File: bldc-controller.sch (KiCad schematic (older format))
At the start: 13 parts

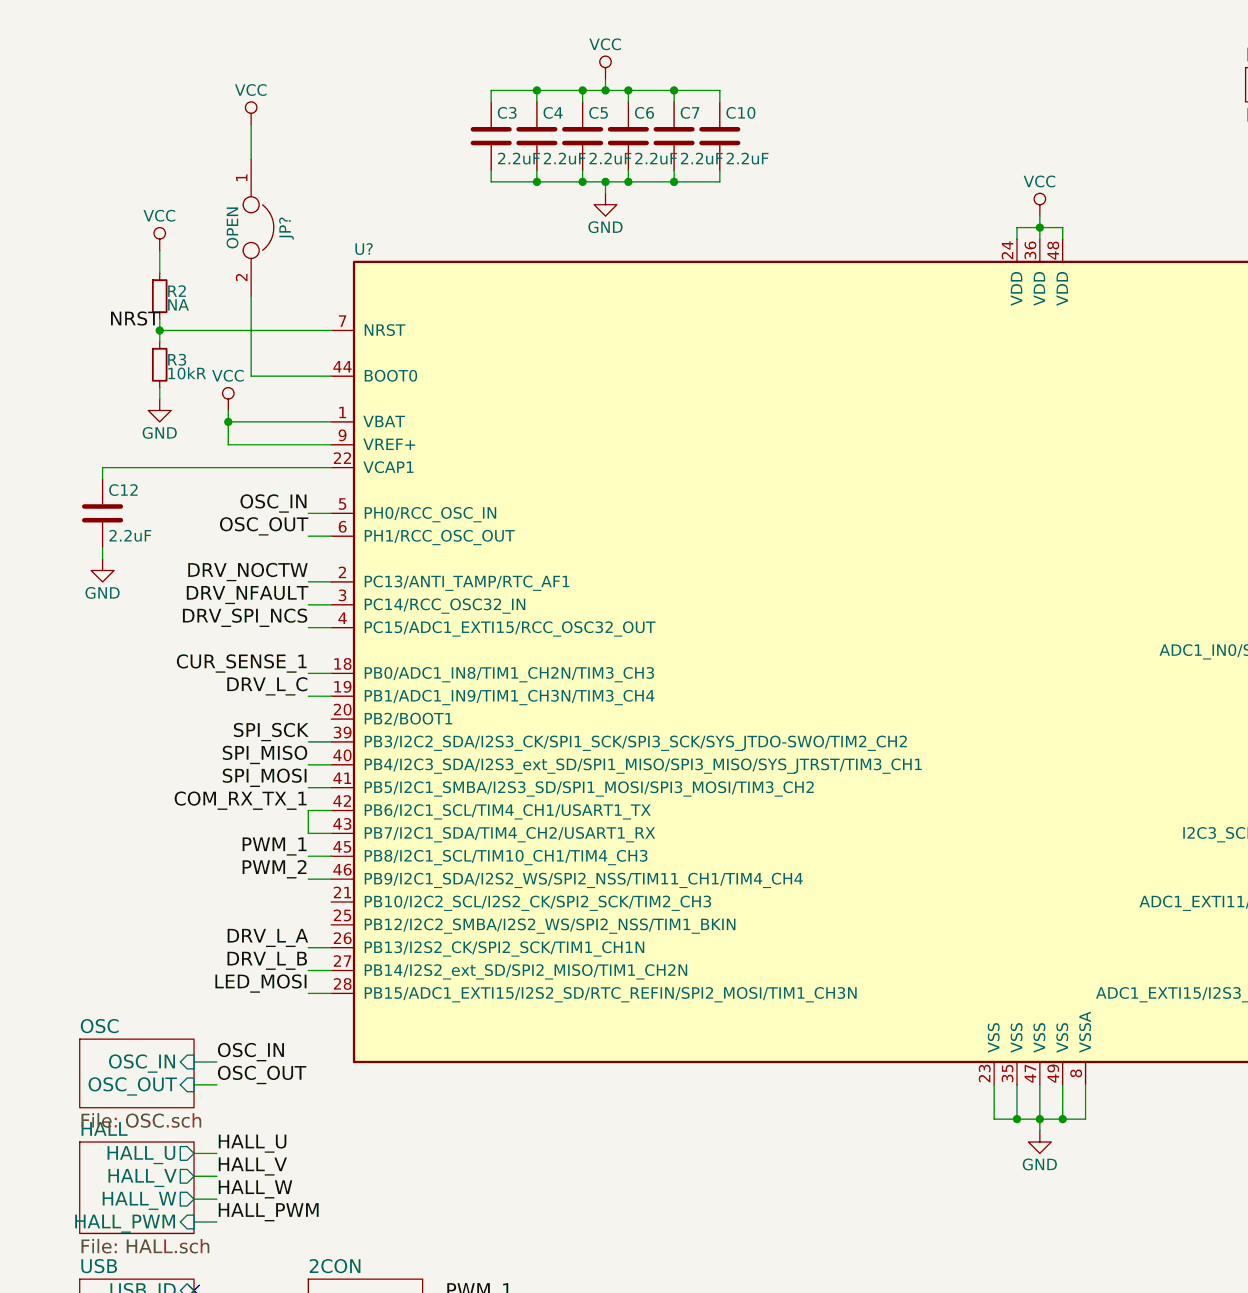
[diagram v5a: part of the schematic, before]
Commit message: changed the maximum outpul voltage of the RC-Filter to VPP
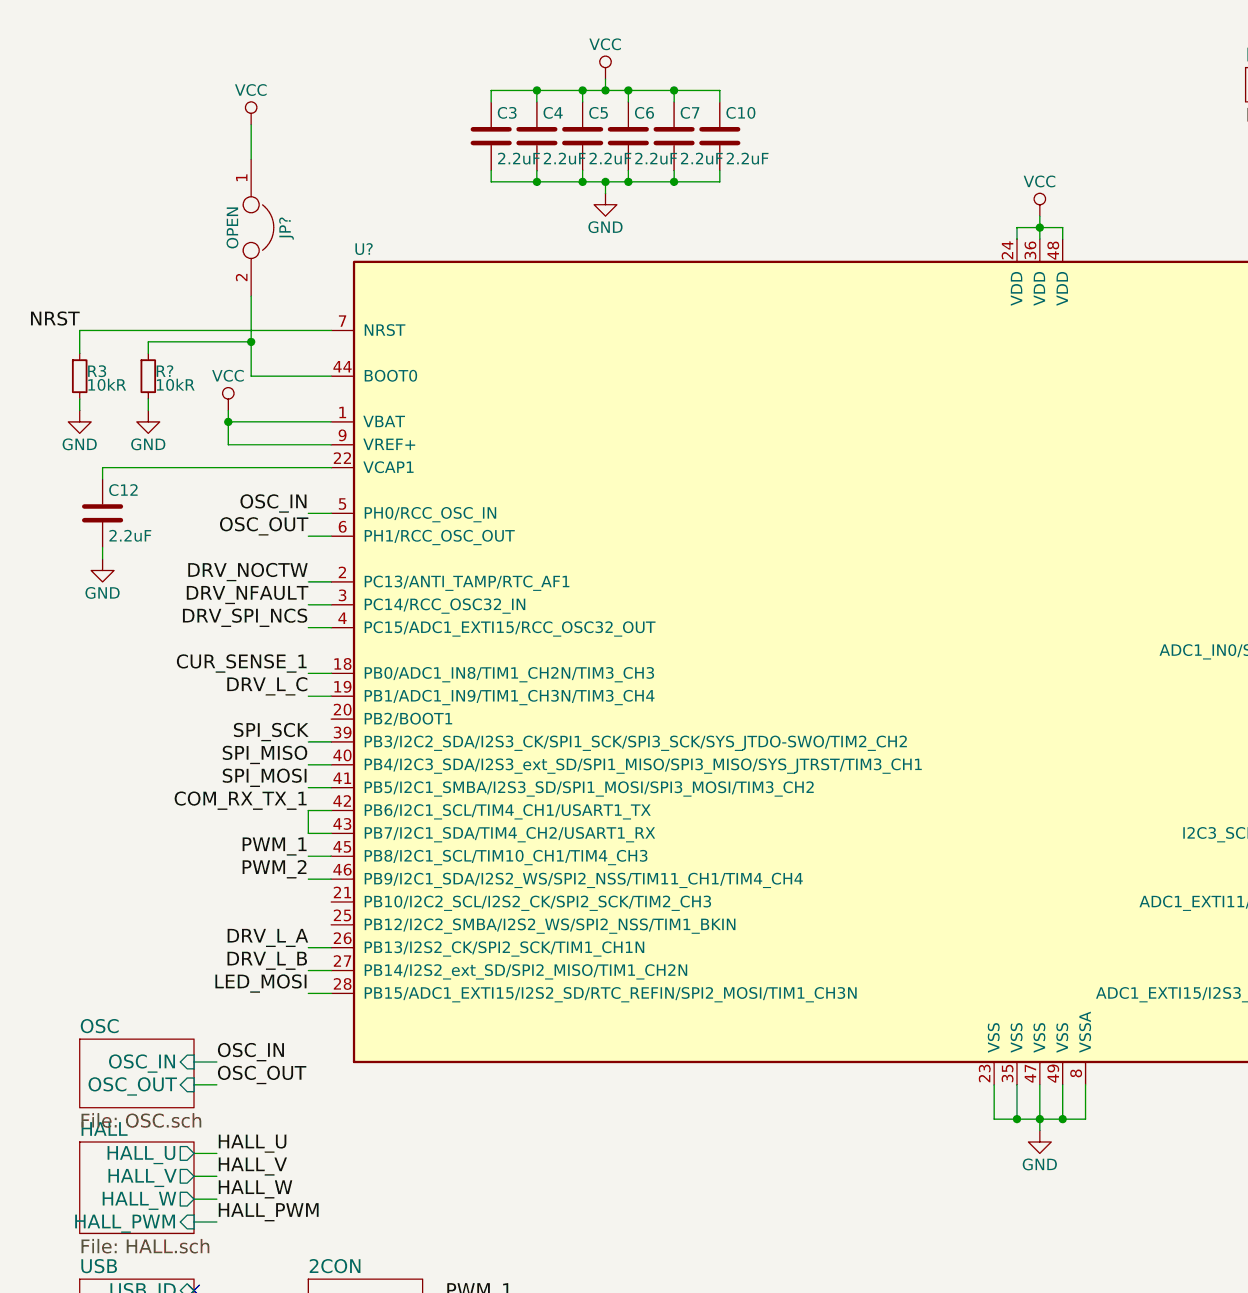
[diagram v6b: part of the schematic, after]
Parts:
- removed R2: NA, Resistors_SMD:R_0603, symbol R_Small
- added R?: 10kR, Resistors_SMD:R_0603, symbol R_Small
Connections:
- net GND: now also R?.2
- net at JP?.2, U?.44 (BOOT0): now also R?.1
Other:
- moved on the sheet: R3
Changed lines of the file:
@@
-$EndComp
-$Comp
-L GND #PWR02
-U 1 1 578D600F
-P 1050 2150
-F 0 "#PWR02" H 1050 1900 50  0001 C CNN
-F 1 "GND" H 1050 2000 50  0000 C CNN
-F 2 "" H 1050 2150 50  0000 C CNN
-F 3 "" H 1050 2150 50  0000 C CNN
-	1    1050 2150
-	1    0    0    -1
-$EndComp
-$Comp
-L R_Small R2
-U 1 1 578E3133
-P 1050 1700
-F 0 "R2" H 1080 1720 50  0000 L CNN
-F 1 "NA" H 1080 1660 50  0000 L CNN
-F 2 "Resistors_SMD:R_0603" H 1050 1700 50  0001 C CNN
-F 3 "" H 1050 1700 50  0000 C CNN
-	1    1050 1700
-	1    0    0    -1
-$EndComp
-$Comp
-L R_Small R3
-U 1 1 578E3167
-P 1050 2000
-F 0 "R3" H 1080 2020 50  0000 L CNN
-F 1 "10kR" H 1080 1960 50  0000 L CNN
-F 2 "Resistors_SMD:R_0603" H 1050 2000 50  0001 C CNN
-F 3 "" H 1050 2000 50  0000 C CNN
-	1    1050 2000
-	1    0    0    -1
-$EndComp
-$Comp
-L VCC #PWR03
-U 1 1 578E31E6
-P 1050 1500
-F 0 "#PWR03" H 1050 1350 50  0001 C CNN
-F 1 "VCC" H 1050 1650 50  0000 C CNN
-F 2 "" H 1050 1500 50  0000 C CNN
-F 3 "" H 1050 1500 50  0000 C CNN
-	1    1050 1500
-	1    0    0    -1
 $EndComp
 $Comp
@@
 Text Label 1300 6800 0    60   ~ 0
 NRST
-Text Label 1050 1850 2    60   ~ 0
+Text Label 700  1850 2    60   ~ 0
 NRST
 $Comp
@@
 	4800 1400 4800 1450
 Wire Wire Line
-	4800 1400 5000 1400
-Wire Wire Line
-	4900 1350 4900 1450
+	4800 1400 4900 1400
+Wire Wire Line
+	4900 1400 5000 1400
+Wire Wire Line
+	4900 1350 4900 1400
+Wire Wire Line
+	4900 1400 4900 1450
 Wire Wire Line
 	2200 6200 2300 6200
@@
 	4700 5150 4700 5300
 Wire Wire Line
-	4700 5300 5100 5300
-Wire Wire Line
-	4900 5150 4900 5350
+	4700 5300 4800 5300
+Wire Wire Line
+	4800 5300 4900 5300
+Wire Wire Line
+	4900 5300 5000 5300
+Wire Wire Line
+	5000 5300 5100 5300
+Wire Wire Line
+	4900 5150 4900 5300
+Wire Wire Line
+	4900 5300 4900 5350
 Wire Wire Line
 	1700 2750 1800 2750
@@
 	3500 1200 3500 1150
 Wire Wire Line
-	2500 1200 3500 1200
+	2500 1200 2700 1200
+Wire Wire Line
+	2700 1200 2900 1200
+Wire Wire Line
+	2900 1200 3000 1200
+Wire Wire Line
+	3000 1200 3100 1200
+Wire Wire Line
+	3100 1200 3300 1200
+Wire Wire Line
+	3300 1200 3500 1200
 Connection ~ 2700 800
 Wire Wire Line
@@
 	3500 800  3500 850
 Wire Wire Line
-	2500 800  3500 800
-Wire Wire Line
-	1450 1700 1450 2050
+	2500 800  2700 800
+Wire Wire Line
+	2700 800  2900 800
+Wire Wire Line
+	2900 800  3000 800
+Wire Wire Line
+	3000 800  3100 800
+Wire Wire Line
+	3100 800  3300 800
+Wire Wire Line
+	3300 800  3500 800
+Wire Wire Line
+	1450 1700 1450 1900
+Wire Wire Line
+	1450 1900 1450 2050
 Wire Wire Line
 	1450 950  1450 1100
-Connection ~ 1050 1850
-Wire Wire Line
-	1050 1500 1050 1600
-Wire Wire Line
-	1050 1800 1050 1900
-Wire Wire Line
-	1050 2150 1050 2100
-Wire Wire Line
-	1050 1850 1800 1850
+Wire Wire Line
+	700  1850 1800 1850
 Wire Wire Line
 	8100 3450 8000 3450
@@
 	1700 3150 1800 3150
 Wire Wire Line
-	1350 2200 1350 2350
+	1350 2200 1350 2250
+Wire Wire Line
+	1350 2250 1350 2350
 Wire Wire Line
 	1350 2250 1800 2250
@@
 Wire Wire Line
 	1700 4750 1800 4750
+Wire Wire Line
+	700  1950 700  1850
+Wire Wire Line
+	700  2200 700  2150
+$Comp
+L R_Small R3
+U 1 1 578E3167
+P 700 2050
+F 0 "R3" H 730 2070 50  0000 L CNN
+F 1 "10kR" H 730 2010 50  0000 L CNN
+F 2 "Resistors_SMD:R_0603" H 700 2050 50  0001 C CNN
+F 3 "" H 700 2050 50  0000 C CNN
+	1    700  2050
+	1    0    0    -1
+$EndComp
+$Comp
+L GND #PWR02
+U 1 1 578D600F
+P 700 2200
+F 0 "#PWR02" H 700 1950 50  0001 C CNN
+F 1 "GND" H 700 2050 50  0000 C CNN
+F 2 "" H 700 2200 50  0000 C CNN
+F 3 "" H 700 2200 50  0000 C CNN
+	1    700  2200
+	1    0    0    -1
+$EndComp
+Wire Wire Line
+	1000 2200 1000 2150
+$Comp
+L R_Small R?
+U 1 1 580F426E
+P 1000 2050
+F 0 "R?" H 1030 2070 50  0000 L CNN
+F 1 "10kR" H 1030 2010 50  0000 L CNN
+F 2 "Resistors_SMD:R_0603" H 1000 2050 50  0001 C CNN
+F 3 "" H 1000 2050 50  0000 C CNN
+	1    1000 2050
+	1    0    0    -1
+$EndComp
+$Comp
+L GND #PWR?
+U 1 1 580F4274
+P 1000 2200
+F 0 "#PWR?" H 1000 1950 50  0001 C CNN
+F 1 "GND" H 1000 2050 50  0000 C CNN
+F 2 "" H 1000 2200 50  0000 C CNN
+F 3 "" H 1000 2200 50  0000 C CNN
+	1    1000 2200
+	1    0    0    -1
+$EndComp
+Wire Wire Line
+	1000 1950 1000 1900
+Wire Wire Line
+	1000 1900 1450 1900
+Connection ~ 1450 1900
 $EndSCHEMATC

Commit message: routed... at least for now
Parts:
- added C1: 100nF, Capacitors_SMD:C_0603, symbol C_Small
- JP1: renamed from JP?; footprint (none) -> Resistors_SMD:R_0402
- U1: renamed from U?; footprint UFQFPN48 -> Housings_DFN_QFN:QFN-48-1EP_7x7mm_Pitch0.5mm
- gave numbers to parts that had none: 1
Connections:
- net COM_RX_TX_1: no longer U1.42 (PB6/I2C1_SCL/TIM4_CH1/USART1_TX)
- net DRV_DC_CAL: now also U1.21 (PB10/I2C2_SCL/I2S2_CK/SPI2_SCK/TIM2_CH3)
- net DRV_ENABLE: now also U1.25 (PB12/I2C2_SMBA/I2S2_WS/SPI2_NSS/TIM1_BKIN)
- net GND: now also C1.2; no longer R3.2
- net SENSE_V_1: now also U1.17 (ADC1_IN7/SPI1_MOSI/TIM1_CH1N/TIM3_CH2/PA7); no longer U1.15 (ADC1_IN5/SPI1_SCK/TIM2_CH1/TIM2_ETR/PA5)
- net SENSE_V_3: now also U1.15 (ADC1_IN5/SPI1_SCK/TIM2_CH1/TIM2_ETR/PA5); no longer U1.17 (ADC1_IN7/SPI1_MOSI/TIM1_CH1N/TIM3_CH2/PA7)
- net VCC: now also R3.2
- net BOOT: now reaches JP1.2, R1.1, U1.44 (BOOT0)
- net BOOT: now also U1.42 (PB6/I2C1_SCL/TIM4_CH1/USART1_TX), C1.1
- net CUR_SENSE_2 renamed V_PP_SENSE
- net USB_DM renamed USB_D-
- net USB_DP renamed USB_D+
- no-connect marks 1 -> 2
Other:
- moved on the sheet: R3
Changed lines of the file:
@@
 $EndComp
 $Comp
-L GND #PWR04
+L GND #PWR02
 U 1 1 578E393F
 P 3000 1250
-F 0 "#PWR04" H 3000 1000 50  0001 C CNN
+F 0 "#PWR02" H 3000 1000 50  0001 C CNN
 F 1 "GND" H 3000 1100 50  0000 C CNN
 F 2 "" H 3000 1250 50  0000 C CNN
@@
 $EndComp
 $Comp
-L VCC #PWR05
+L VCC #PWR03
 U 1 1 578E39A1
 P 3000 750
-F 0 "#PWR05" H 3000 600 50  0001 C CNN
+F 0 "#PWR03" H 3000 600 50  0001 C CNN
 F 1 "VCC" H 3000 900 50  0000 C CNN
 F 2 "" H 3000 750 50  0000 C CNN
@@
 $EndComp
 $Comp
-L VCC #PWR06
+L VCC #PWR04
 U 1 1 578E3BA4
 P 1450 950
-F 0 "#PWR06" H 1450 800 50  0001 C CNN
+F 0 "#PWR04" H 1450 800 50  0001 C CNN
 F 1 "VCC" H 1450 1100 50  0000 C CNN
 F 2 "" H 1450 950 50  0000 C CNN
@@
 $EndSheet
 $Comp
-L GND #PWR07
+L GND #PWR05
 U 1 1 578E83F1
 P 4900 5350
-F 0 "#PWR07" H 4900 5100 50  0001 C CNN
+F 0 "#PWR05" H 4900 5100 50  0001 C CNN
 F 1 "GND" H 4900 5200 50  0000 C CNN
 F 2 "" H 4900 5350 50  0000 C CNN
@@
 $EndSheet
 Text Label 1300 6150 0    60   ~ 0
-USB_DP
+USB_D+
 Text Label 1300 6250 0    60   ~ 0
-USB_DM
+USB_D-
 NoConn ~ 1200 6050
 Text Label 8100 4450 0    60   ~ 0
-USB_DP
+USB_D+
 Text Label 8100 4350 0    60   ~ 0
-USB_DM
+USB_D-
 $Sheet
 S 700  6550 500  350
@@
 $EndComp
 $Comp
-L VCC #PWR010
+L VCC #PWR06
 U 1 1 578F4438
 P 9000 4700
-F 0 "#PWR010" H 9000 4550 50  0001 C CNN
+F 0 "#PWR06" H 9000 4550 50  0001 C CNN
 F 1 "VCC" H 9000 4850 50  0000 C CNN
 F 2 "" H 9000 4700 50  0000 C CNN
@@
 	1    0    0    -1
 $EndComp
-Text Label 1700 3950 2    60   ~ 0
+Text Label 1700 4050 2    60   ~ 0
 COM_RX_TX_1
 $Sheet
@@
 F6 "OUT_2" O R 10550 750 60
 F7 "OUT_3" O R 10550 900 60
-$EndSheet
-Text Label 9500 900  2    60   ~ 0
+F8 "IN_4" I L 9550 1000 60
+F9 "OUT_4" O R 10550 1000 60
+$EndSheet
+Text Label 9500 650  2    60   ~ 0
 DRV_OUT_1
 Text Label 9500 750  2    60   ~ 0
 DRV_OUT_2
-Text Label 9500 650  2    60   ~ 0
-DRV_OUT_2
+Text Label 9500 900  2    60   ~ 0
+DRV_OUT_3
 Text Label 10600 650  0    60   ~ 0
 SENSE_V_1
@@
 PWM_2
 $Comp
-L STM32F401CBUx U?
+L STM32F401CBUx U1
 U 1 1 5807ABBD
 P 4900 3350
-F 0 "U?" H 1900 5175 50  0000 L BNN
+F 0 "U1" H 1900 5175 50  0000 L BNN
 F 1 "STM32F401CBUx" H 7900 5175 50  0000 R BNN
-F 2 "UFQFPN48" H 7900 5125 50  0000 R TNN
+F 2 "Housings_DFN_QFN:QFN-48-1EP_7x7mm_Pitch0.5mm" H 7900 5125 50  0000 R TNN
 F 3 "" H 4900 3350 50  0000 C CNN
 	1    4900 3350
@@
 F19 "DRV_SDO" B R 5550 6850 60
 F20 "DRV_CUR_1" O R 5550 7250 60
-F21 "DRV_CUR_2" O R 5550 7350 60
 $EndSheet
 Text Label 4000 6700 2    60   ~ 0
@@
 SWDCLK
 $Comp
-L GND #PWR?
+L GND #PWR07
 U 1 1 580BEB44
 P 800 2850
-F 0 "#PWR?" H 800 2600 50  0001 C CNN
+F 0 "#PWR07" H 800 2600 50  0001 C CNN
 F 1 "GND" H 800 2700 50  0000 C CNN
 F 2 "" H 800 2850 50  0000 C CNN
@@
 $EndComp
 $Comp
-L VCC #PWR?
+L VCC #PWR08
 U 1 1 580C0FAE
 P 6500 6900
-F 0 "#PWR?" H 6500 6750 50  0001 C CNN
+F 0 "#PWR08" H 6500 6750 50  0001 C CNN
 F 1 "VCC" H 6500 7050 50  0000 C CNN
 F 2 "" H 6500 6900 50  0000 C CNN
@@
 Text Label 5650 7250 0    60   ~ 0
 CUR_SENSE_1
-Text Label 5650 7350 0    60   ~ 0
-CUR_SENSE_2
 Text Label 5650 7050 0    60   ~ 0
 DRV_DC_CAL
@@
 CUR_SENSE_1
 Text Label 8100 3650 0    60   ~ 0
-CUR_SENSE_2
-$Comp
-L JUMPER JP?
+V_PP_SENSE
+$Comp
+L JUMPER JP1
 U 1 1 580CCA9A
 P 1450 1400
-F 0 "JP?" H 1450 1550 50  0000 C CNN
+F 0 "JP1" H 1450 1550 50  0000 C CNN
 F 1 "OPEN" H 1450 1320 50  0000 C CNN
-F 2 "" H 1450 1400 50  0000 C CNN
+F 2 "Resistors_SMD:R_0402" H 1450 1400 50  0001 C CNN
 F 3 "" H 1450 1400 50  0000 C CNN
 	1    1450 1400
 	0    1    1    0
 $EndComp
-Text Label 8100 3750 0    60   ~ 0
+Text Label 8100 3950 0    60   ~ 0
 SENSE_V_1
 Text Label 8100 3850 0    60   ~ 0
 SENSE_V_2
-Text Label 8100 3950 0    60   ~ 0
+Text Label 8100 3750 0    60   ~ 0
 SENSE_V_3
 $Comp
-L VCC #PWR?
+L VCC #PWR09
 U 1 1 580D5C32
 P 1350 2200
-F 0 "#PWR?" H 1350 2050 50  0001 C CNN
+F 0 "#PWR09" H 1350 2050 50  0001 C CNN
 F 1 "VCC" H 1350 2350 50  0000 C CNN
 F 2 "" H 1350 2200 50  0000 C CNN
@@
 	4800 1400 4800 1450
 Wire Wire Line
-	4800 1400 4900 1400
-Wire Wire Line
-	4900 1400 5000 1400
-Wire Wire Line
-	4900 1350 4900 1400
-Wire Wire Line
-	4900 1400 4900 1450
+	4800 1400 5000 1400
+Wire Wire Line
+	4900 1350 4900 1450
 Wire Wire Line
 	2200 6200 2300 6200
@@
 	9500 650  9550 650
 Wire Wire Line
-	1700 4050 1700 3950
-Wire Wire Line
 	1800 4050 1700 4050
 Wire Wire Line
@@
 Wire Wire Line
 	9000 4700 9000 4750
-Wire Wire Line
-	1700 3950 1800 3950
 Wire Wire Line
 	8750 4750 8600 4750
@@
 	4700 5150 4700 5300
 Wire Wire Line
-	4700 5300 4800 5300
-Wire Wire Line
-	4800 5300 4900 5300
-Wire Wire Line
-	4900 5300 5000 5300
-Wire Wire Line
-	5000 5300 5100 5300
-Wire Wire Line
-	4900 5150 4900 5300
-Wire Wire Line
-	4900 5300 4900 5350
+	4700 5300 5100 5300
+Wire Wire Line
+	4900 5150 4900 5350
 Wire Wire Line
 	1700 2750 1800 2750
@@
 	3500 1200 3500 1150
 Wire Wire Line
-	2500 1200 2700 1200
-Wire Wire Line
-	2700 1200 2900 1200
-Wire Wire Line
-	2900 1200 3000 1200
-Wire Wire Line
-	3000 1200 3100 1200
-Wire Wire Line
-	3100 1200 3300 1200
-Wire Wire Line
-	3300 1200 3500 1200
+	2500 1200 3500 1200
 Connection ~ 2700 800
 Wire Wire Line
@@
 	3500 800  3500 850
 Wire Wire Line
-	2500 800  2700 800
-Wire Wire Line
-	2700 800  2900 800
-Wire Wire Line
-	2900 800  3000 800
-Wire Wire Line
-	3000 800  3100 800
-Wire Wire Line
-	3100 800  3300 800
-Wire Wire Line
-	3300 800  3500 800
-Wire Wire Line
-	1450 1700 1450 1900
-Wire Wire Line
-	1450 1900 1450 2050
+	2500 800  3500 800
+Wire Wire Line
+	1450 1700 1450 2050
 Wire Wire Line
 	1450 950  1450 1100
@@
 	6500 7150 5550 7150
 Wire Wire Line
-	5650 7350 5550 7350
-Wire Wire Line
 	5550 7250 5650 7250
 Wire Wire Line
@@
 	1700 3150 1800 3150
 Wire Wire Line
-	1350 2200 1350 2250
-Wire Wire Line
-	1350 2250 1350 2350
+	1350 2200 1350 2350
 Wire Wire Line
 	1350 2250 1800 2250
@@
 Wire Wire Line
 	1700 4750 1800 4750
-Wire Wire Line
-	700  1950 700  1850
-Wire Wire Line
-	700  2200 700  2150
 $Comp
 L R_Small R3
 U 1 1 578E3167
-P 700 2050
-F 0 "R3" H 730 2070 50  0000 L CNN
-F 1 "10kR" H 730 2010 50  0000 L CNN
-F 2 "Resistors_SMD:R_0603" H 700 2050 50  0001 C CNN
-F 3 "" H 700 2050 50  0000 C CNN
-	1    700  2050
-	1    0    0    -1
-$EndComp
-$Comp
-L GND #PWR02
-U 1 1 578D600F
-P 700 2200
-F 0 "#PWR02" H 700 1950 50  0001 C CNN
-F 1 "GND" H 700 2050 50  0000 C CNN
-F 2 "" H 700 2200 50  0000 C CNN
-F 3 "" H 700 2200 50  0000 C CNN
-	1    700  2200
-	1    0    0    -1
+P 700 1650
+F 0 "R3" H 730 1670 50  0000 L CNN
+F 1 "10kR" H 730 1610 50  0000 L CNN
+F 2 "Resistors_SMD:R_0603" H 700 1650 50  0001 C CNN
+F 3 "" H 700 1650 50  0000 C CNN
+	1    700  1650
+	-1   0    0    1
 $EndComp
 Wire Wire Line
 	1000 2200 1000 2150
 $Comp
-L R_Small R?
+L R_Small R1
 U 1 1 580F426E
 P 1000 2050
-F 0 "R?" H 1030 2070 50  0000 L CNN
+F 0 "R1" H 1030 2070 50  0000 L CNN
 F 1 "10kR" H 1030 2010 50  0000 L CNN
 F 2 "Resistors_SMD:R_0603" H 1000 2050 50  0001 C CNN
@@
 $EndComp
 $Comp
-L GND #PWR?
+L GND #PWR010
 U 1 1 580F4274
 P 1000 2200
-F 0 "#PWR?" H 1000 1950 50  0001 C CNN
+F 0 "#PWR010" H 1000 1950 50  0001 C CNN
 F 1 "GND" H 1000 2050 50  0000 C CNN
 F 2 "" H 1000 2200 50  0000 C CNN
@@
 	1000 1900 1450 1900
 Connection ~ 1450 1900
+$Comp
+L C_Small C1
+U 1 1 58126738
+P 1200 2050
+F 0 "C1" H 1210 2120 50  0000 L CNN
+F 1 "100nF" H 1210 1970 50  0000 L CNN
+F 2 "Capacitors_SMD:C_0603" H 1200 2050 50  0001 C CNN
+F 3 "" H 1200 2050 50  0000 C CNN
+	1    1200 2050
+	1    0    0    -1
+$EndComp
+$Comp
+L GND #PWR011
+U 1 1 58126AD7
+P 1200 2200
+F 0 "#PWR011" H 1200 1950 50  0001 C CNN
+F 1 "GND" H 1200 2050 50  0000 C CNN
+F 2 "" H 1200 2200 50  0000 C CNN
+F 3 "" H 1200 2200 50  0000 C CNN
+	1    1200 2200
+	1    0    0    -1
+$EndComp
+Wire Wire Line
+	1200 2200 1200 2150
+Wire Wire Line
+	1200 1950 1200 1900
+Connection ~ 1200 1900
+Text Label 1450 1750 0    60   ~ 0
+BOOT
+Text Label 1700 3950 2    60   ~ 0
+BOOT
+Wire Wire Line
+	1700 3950 1800 3950
+NoConn ~ 1800 3550
+Text Label 1700 4450 2    60   ~ 0
+DRV_ENABLE
+Wire Wire Line
+	1700 4450 1800 4450
+Text Label 1700 4350 2    60   ~ 0
+DRV_DC_CAL
+Wire Wire Line
+	1700 4350 1800 4350
+$Comp
+L VCC #PWR012
+U 1 1 58138DD1
+P 700 1450
+F 0 "#PWR012" H 700 1300 50  0001 C CNN
+F 1 "VCC" H 700 1600 50  0000 C CNN
+F 2 "" H 700 1450 50  0000 C CNN
+F 3 "" H 700 1450 50  0000 C CNN
+	1    700  1450
+	1    0    0    -1
+$EndComp
+Wire Wire Line
+	700  1850 700  1750
+Wire Wire Line
+	700  1550 700  1450
+Text Label 10600 1000 0    60   ~ 0
+V_PP_SENSE
+Wire Wire Line
+	10600 1000 10550 1000
+$Comp
+L VPP #PWR013
+U 1 1 5817D479
+P 8900 900
+F 0 "#PWR013" H 8900 750 50  0001 C CNN
+F 1 "VPP" H 8900 1050 50  0000 C CNN
+F 2 "" H 8900 900 50  0000 C CNN
+F 3 "" H 8900 900 50  0000 C CNN
+	1    8900 900
+	1    0    0    -1
+$EndComp
+Wire Wire Line
+	8900 900  8900 1000
+Wire Wire Line
+	8900 1000 9550 1000
 $EndSCHEMATC
